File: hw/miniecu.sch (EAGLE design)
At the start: 59 parts

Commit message: use two resistors in voltage divider
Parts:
- added R20: 10k, resistor:R-EU_R0805
- R10, R13, R17: value np -> 10k
- R12: value 10k -> np; device resistor:R-EU_R0805 -> resistor:R-EU_R0603
- R14: value 100 -> np; device resistor:R-EU_R0603 -> resistor:R-EU_R0805
- R16: value 10k -> 100; device resistor:R-EU_R0805 -> resistor:R-EU_R0603
- R18: value 5.1k -> np; device resistor:R-EU_R0603 -> resistor:R-EU_R0805
- R19: value 10k -> 5.1k; device resistor:R-EU_R0805 -> resistor:R-EU_R0603
- R5: device resistor:R-EU_R0603 -> resistor:R-EU_R0805
- R6: value 140 -> 10k
- R7: value 10k -> 140; device resistor:R-EU_R0805 -> resistor:R-EU_R0603
- R8: value 100 -> 10k; device resistor:R-EU_R0603 -> resistor:R-EU_R0805
- R9: value 10k -> 100
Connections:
- new net N$1: R3.1, R4.2
- net +3V3: now also R20.2, R6.2; no longer R19.2, R5.2
- net AGND: now also R14.1, R18.1; no longer R13.1, R17.1
- net AVCC_EXT: now also R13.2, R17.2; no longer R12.2, R16.2
- net FLOW_PULSE: now also R12.2, R16.1; no longer R11.2, R15.1
- net GND: now also R12.1, R19.1, R5.1, R8.2; no longer R18.1, R4.1, R7.2, R9.1
- net IGN_EN: now also R9.1; no longer R8.1
- net I_SENSE: now also R8.1; no longer R7.1
- net LED: now also R7.1; no longer R6.1
- net N$2: now also R7.2; no longer R6.2
- net N$3: now also R6.1; no longer R5.1
- net N$4: now also R16.2, R20.1; no longer R15.2, R19.1
- net N$7: now also R9.2; no longer R8.2
- net N$9: now also R10.2; no longer R9.2
- net OIL_PRES: now also R17.1, R18.2; no longer R16.1, R17.2
- net RPM_IN: now also R11.2, R15.1; no longer R10.2, R14.1
- net RPM_IN_CON: now also R15.2; no longer R14.2
- net STARTER: now also R19.2; no longer R18.2
- net THERM: now also R13.1, R14.2; no longer R12.1, R13.2
- net V_SENSE: now also R4.1, R5.2; no longer R3.1, R4.2
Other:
- moved on the sheet: C4, H1, H2, R10, R11, R12, R13, R14, R15, R16, R17, R18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

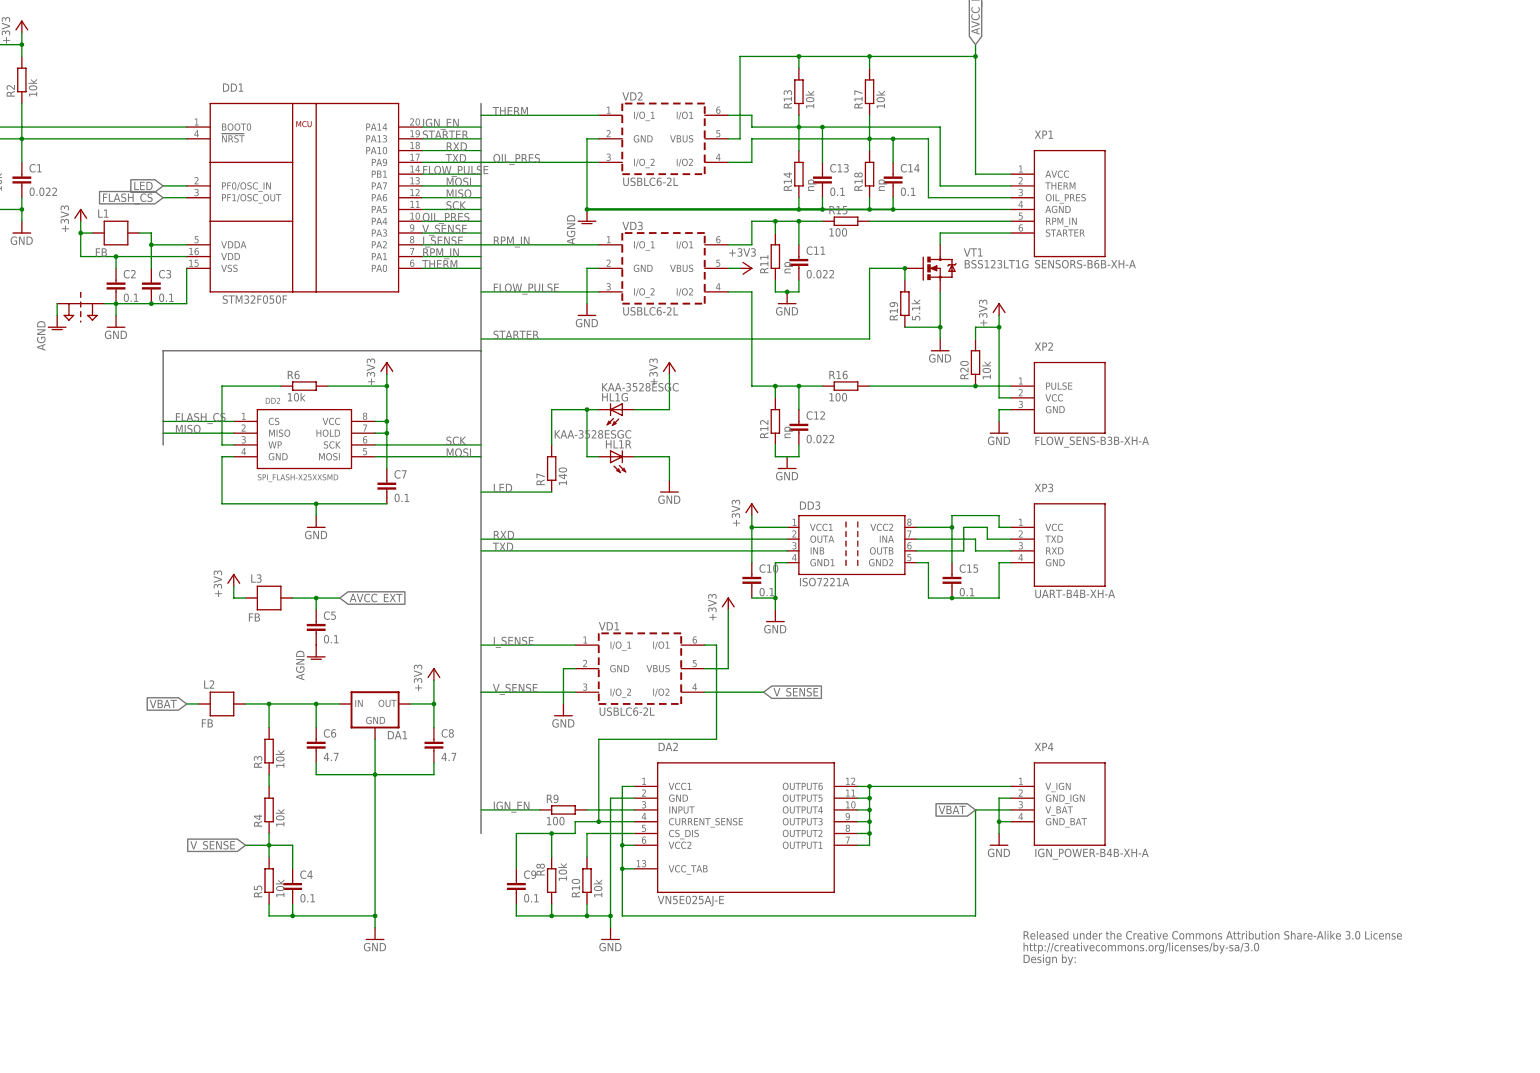
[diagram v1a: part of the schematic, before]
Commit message: pcb: routing done
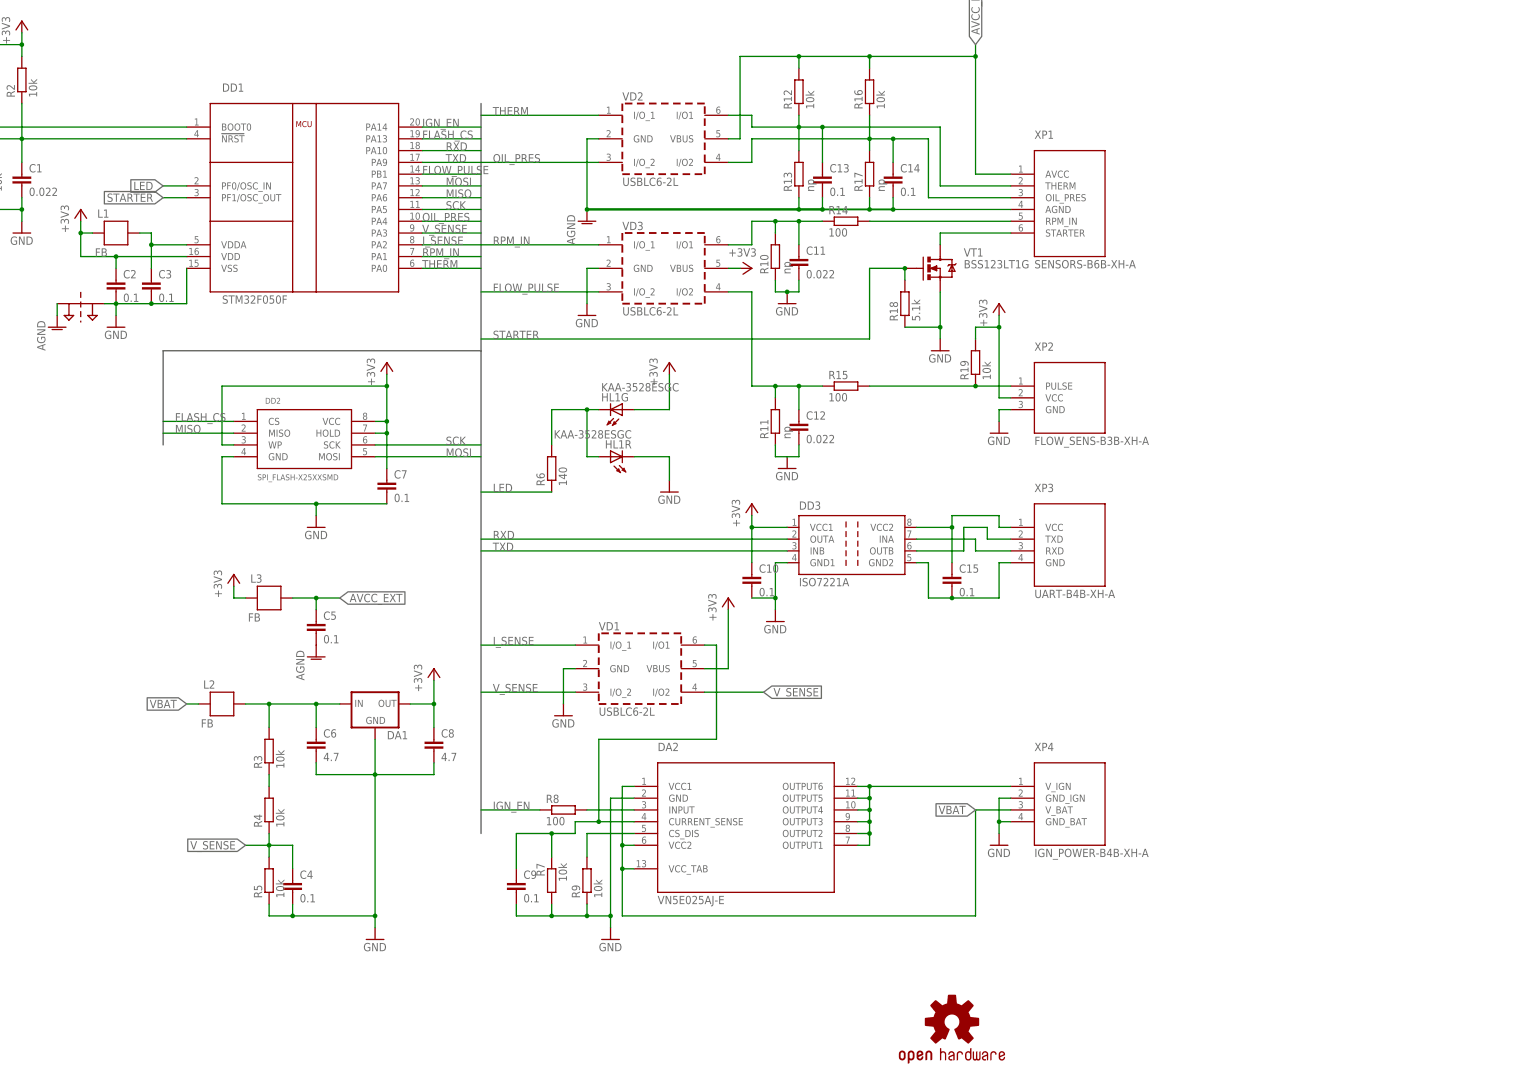
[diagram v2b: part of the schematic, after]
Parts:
- removed R20: 10k, resistor:R-EU_R0805
- removed U$1: CREATIVE_COMMONS_BY-SA, logo:CREATIVE_COMMONS_BY-SA
- added LOGO1: OSHW-LOGOL, SparkFun-Aesthetics:OSHW-LOGOL
- R10, R13, R17: value 10k -> np
- R12: value np -> 10k; device resistor:R-EU_R0603 -> resistor:R-EU_R0805
- R14: value np -> 100; device resistor:R-EU_R0805 -> resistor:R-EU_R0603
- R16: value 100 -> 10k; device resistor:R-EU_R0603 -> resistor:R-EU_R0805
- R18: value np -> 5.1k; device resistor:R-EU_R0805 -> resistor:R-EU_R0603
- R19: value 5.1k -> 10k; device resistor:R-EU_R0603 -> resistor:R-EU_R0805
- R6: value 10k -> 140
- R7: value 140 -> 10k; device resistor:R-EU_R0603 -> resistor:R-EU_R0805
- R8: value 10k -> 100; device resistor:R-EU_R0805 -> resistor:R-EU_R0603
- R9: value 100 -> 10k
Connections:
- removed net N$3: DD2.WP, R6.1
- net +3V3: now also DD2.WP, R19.2; no longer R20.2, R6.2
- net AGND: now also R13.1, R17.1; no longer R14.1, R18.1
- net AVCC_EXT: now also R12.2, R16.2; no longer R13.2, R17.2
- net FLASH_CS: now also DD1.PA13; no longer DD1.PF1/OSC_OUT
- net FLOW_PULSE: now also R11.2, R15.1; no longer R12.2, R16.1
- net GND: now also R18.1, R7.2, R9.1; no longer R12.1, R19.1, R8.2
- net IGN_EN: now also R8.1; no longer R9.1
- net I_SENSE: now also R7.1; no longer R8.1
- net LED: now also R6.1; no longer R7.1
- net N$2: now also R6.2; no longer R7.2
- net N$4: now also R15.2, R19.1; no longer R16.2, R20.1
- net N$7: now also R8.2; no longer R9.2
- net N$9: now also R9.2; no longer R10.2
- net OIL_PRES: now also R16.1, R17.2; no longer R17.1, R18.2
- net RPM_IN: now also R10.2, R14.1; no longer R11.2, R15.1
- net RPM_IN_CON: now also R14.2; no longer R15.2
- net STARTER: now also DD1.PF1/OSC_OUT, R18.2; no longer DD1.PA13, R19.2
- net THERM: now also R12.1, R13.2; no longer R13.1, R14.2
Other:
- moved on the sheet: R10, R11, R12, R13, R14, R15, R16, R17, R18, R19, R6, R7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

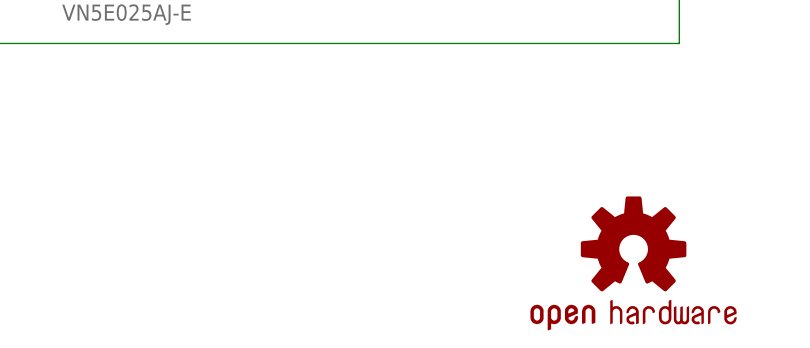
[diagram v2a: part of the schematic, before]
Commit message: add miniECU logo to board
larger logo xcf.
rename miniecu-con.lbr to miniecu.lbr, place symlink for sch.
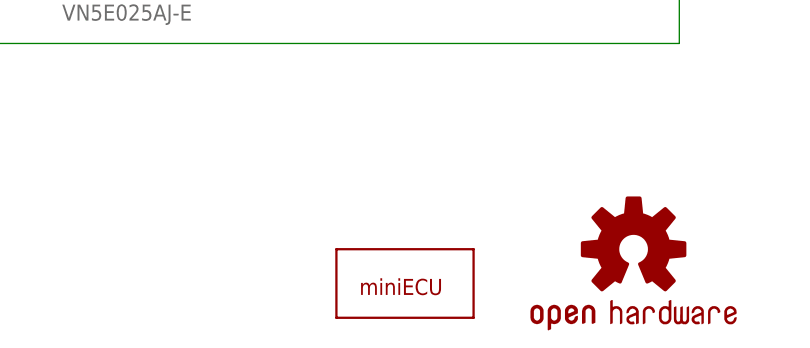
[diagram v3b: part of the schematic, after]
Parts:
- added U$1: MINIECU_LOGO, miniecu:MINIECU_LOGO
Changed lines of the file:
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@@
 <part name="R3" library="resistor" deviceset="R-EU_" device="R0805" value="10k"/>
 <part name="LOGO1" library="SparkFun-Aesthetics" deviceset="OSHW-LOGO" device="L"/>
+<part name="U$1" library="miniecu" deviceset="MINIECU_LOGO" device=""/>
 </parts>
 <sheets>
@@
 <instance part="R3" gate="G$1" x="-10.16" y="-111.76" rot="R90"/>
 <instance part="LOGO1" gate="G$1" x="137.16" y="-170.18"/>
+<instance part="U$1" gate="G$1" x="109.22" y="-175.26"/>
 </instances>
 <busses>

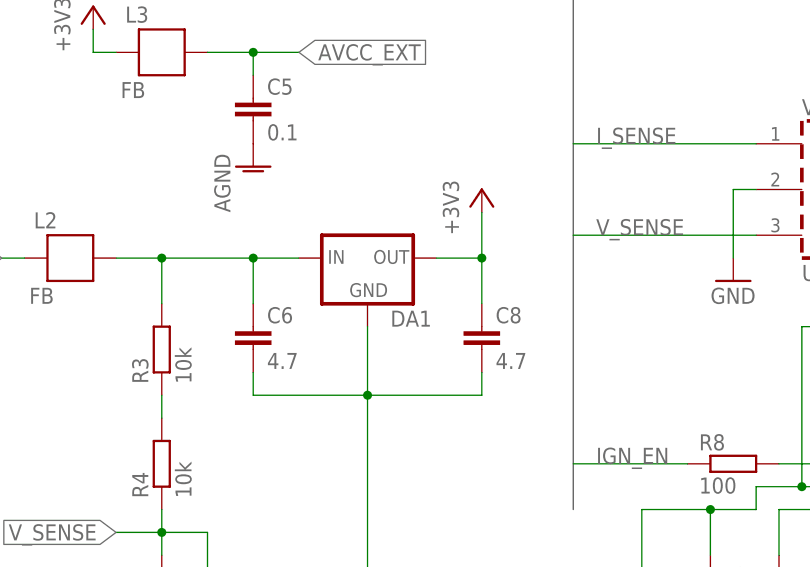
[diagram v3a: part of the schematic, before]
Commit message: sch: change LDO MCP1700 (6V max) -> MCP1703 (16V max) in the same package
Fix LDO ceramic capasitance from 4.7 µF to 1.0 µF (MCP1703 DS)
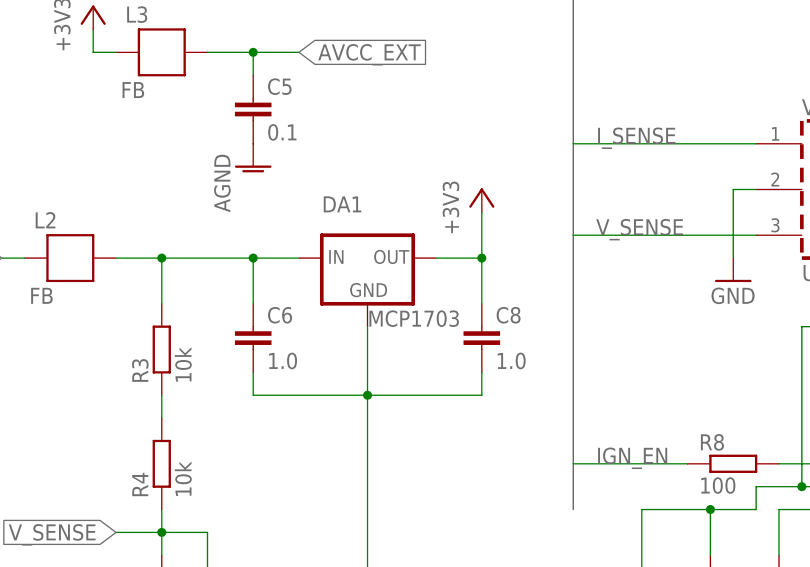
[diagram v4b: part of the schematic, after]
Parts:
- C6, C8: value 4.7 -> 1.0
- DA1: value (none) -> MCP1703
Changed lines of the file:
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@@
 <part name="R6" library="resistor" deviceset="R-EU_" device="R0603" value="140"/>
 <part name="+3V8" library="supply1" deviceset="+3V3" device=""/>
-<part name="DA1" library="power-ic" deviceset="MCP1700" device="SOT-23"/>
+<part name="DA1" library="power-ic" deviceset="MCP1700" device="SOT-23" value="MCP1703"/>
 <part name="L2" library="SparkFun-Passives" deviceset="FB" device=""/>
 <part name="GND11" library="supply1" deviceset="GND" device=""/>
-<part name="C6" library="resistor" deviceset="C-EU" device="C0805" value="4.7"/>
-<part name="C8" library="resistor" deviceset="C-EU" device="C0805" value="4.7"/>
+<part name="C6" library="resistor" deviceset="C-EU" device="C0805" value="1.0"/>
+<part name="C8" library="resistor" deviceset="C-EU" device="C0805" value="1.0"/>
 <part name="+3V9" library="supply1" deviceset="+3V3" device=""/>
 <part name="R4" library="resistor" deviceset="R-EU_" device="R0805" value="10k"/>
@@
 <instance part="R6" gate="G$1" x="50.8" y="-50.8" rot="R90"/>
 <instance part="+3V8" gate="G$1" x="76.2" y="-27.94"/>
-<instance part="DA1" gate="1" x="12.7" y="-101.6"/>
+<instance part="DA1" gate="1" x="12.7" y="-101.6" smashed="yes">
+<attribute name="NAME" x="7.62" y="-96.52" size="1.778" layer="95"/>
+<attribute name="VALUE" x="12.7" y="-109.22" size="1.778" layer="96"/>
+</instance>
 <instance part="L2" gate="G$1" x="-20.32" y="-101.6"/>
 <instance part="GND11" gate="1" x="12.7" y="-152.4"/>
